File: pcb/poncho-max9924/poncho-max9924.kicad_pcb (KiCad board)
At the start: 2 copper layers, 48 parts, among them J1 Screw_Terminal_01x02, J2 Screw_Terminal_01x02, U1 MAX9924, U2 MAX9000

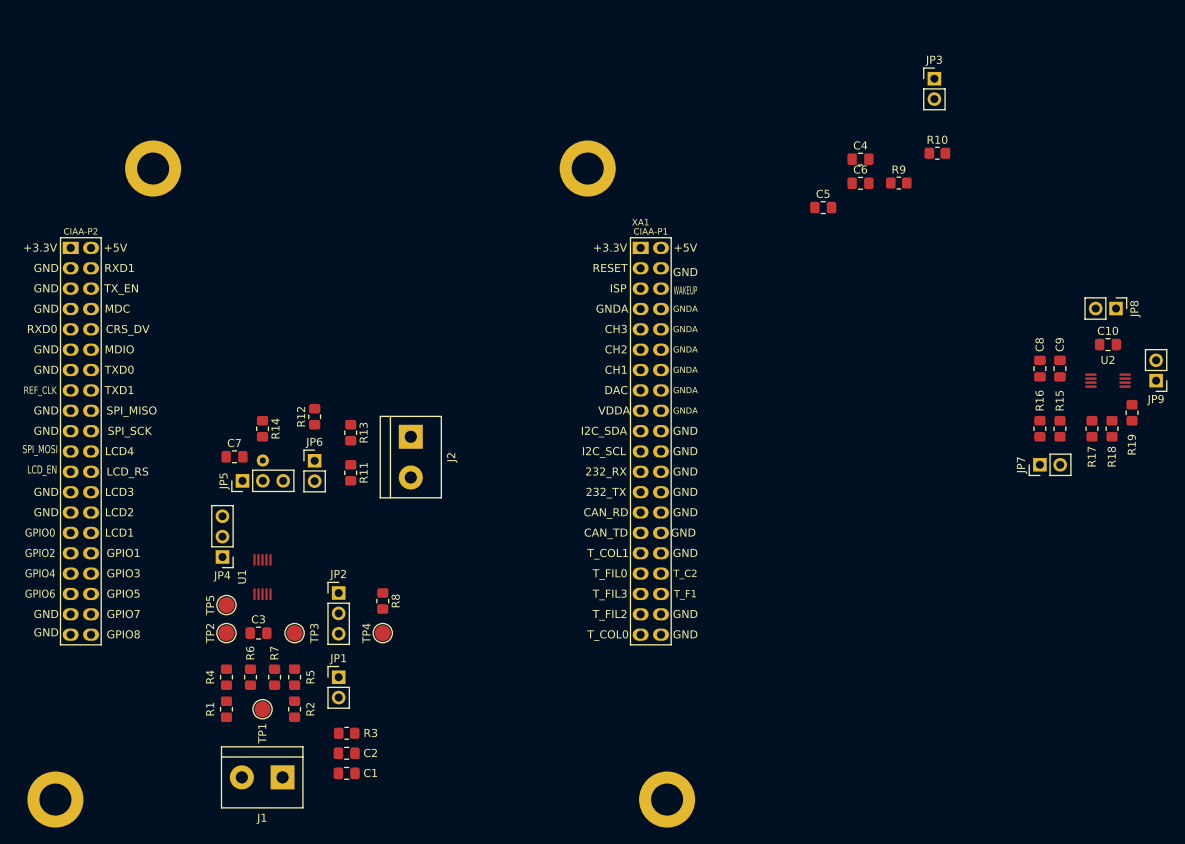
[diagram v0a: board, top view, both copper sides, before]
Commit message: Se agregaron modelos 3D de todos los componentes y sus footprints. Se re trabajo el posicionamiento de componentes en la placa.
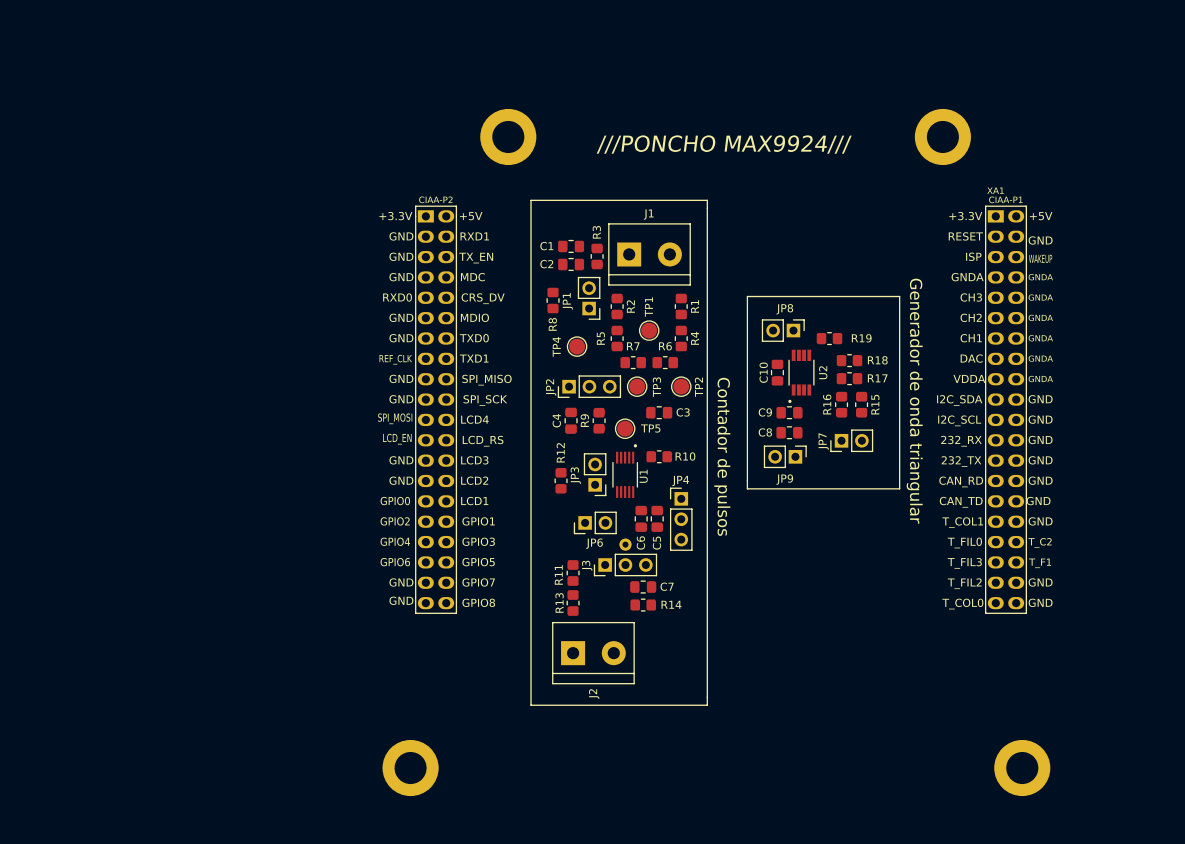
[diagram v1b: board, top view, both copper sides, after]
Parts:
- removed JP5: jumper_4_open, misc:PinHeader_1x03_1x01_P2.54mm_Vertical
- added J3: jumper_4_open, misc:PinHeader_1x03_1x01_P2.54mm_Vertical, F.Cu at (136.2, 112.5)
- U1: footprint umax:UMAX10 -> max9924:SOP50P490X110-10N
- U2: footprint umax:UMAX8 -> max9000:SOP65P490X110-8N
- moved J1 78.3 mm to (139.2, 73.8), turned to 0 degrees
- moved R1 75.8 mm to (145.8, 80.2), turned to 90 degrees
- moved C1 71.5 mm to (132.0, 72.8)
- moved R4 70.8 mm to (145.8, 84.2), turned to 90 degrees
- moved TP1 67.5 mm to (141.8, 83.2), turned to 270 degrees
- moved R3 67.2 mm to (135.2, 74.0), turned to 90 degrees
- moved C2 67.1 mm to (132.0, 75.0)
- moved JP3 66.0 mm to (135.0, 102.5), turned to 180 degrees
- moved R6 65.0 mm to (143.8, 87.2), turned to 180 degrees
- moved TP2 64.5 mm to (145.8, 90.2), turned to 270 degrees
- moved R2 64.4 mm to (137.8, 80.2), turned to 90 degrees
- moved R7 59.5 mm to (139.8, 87.2), turned to 180 degrees
- moved R5 58.4 mm to (137.8, 84.2), turned to 90 degrees
- moved JP4 57.7 mm to (145.8, 104.2), turned to 0 degrees
- moved C3 57.1 mm to (143.0, 93.5), turned to 180 degrees
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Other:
- board text added: "///PONCHO MAX9924///"
- board text added: "Contador de pulsos"
- board text added: "Generador de onda triangular"

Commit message: primer routeado
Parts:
- moved J1 21.4 mm to (144.5, 53.0), turned to 180 degrees
- moved J2 17.2 mm to (115.0, 123.5), turned to 270 degrees
- moved R14 4.47 mm to (137.0, 115.5), turned to 0 degrees
- moved R12 3.51 mm to (131.0, 98.5)
- moved C3 2.00 mm to (143.0, 95.5)
- moved R13 1.77 mm to (132.0, 115.5)
- moved TP3 1.75 mm to (142.0, 90.2)
- moved JP7 1.50 mm to (165.8, 98.5)
- moved R11 1.25 mm to (133.0, 112.5), turned to 0 degrees
- moved R10 1.12 mm to (144.0, 98.5), turned to 90 degrees
- moved C4 1.00 mm to (131.0, 94.5), turned to 90 degrees
- moved C10 0.79 mm to (157.0, 88.2)
- moved R17 0.35 mm to (166.5, 89.0)
- moved C7 0.25 mm to (141.0, 115.5)
- moved R18 0.25 mm to (166.5, 87.0), turned to 180 degrees
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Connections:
- R1 pad 2: Net-(J1-Pad2) -> Net-(J1-Pad1)
- R2 pad 2: Net-(J1-Pad1) -> Net-(J1-Pad2)
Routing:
- net GND: track 0.00 -> 47.3 mm, vias 0 -> 3
- net Net-(C3-Pad2): track 0.00 -> 42.1 mm
- net /AOUT: track 0.00 -> 32.6 mm
- net /COUT: track 0.00 -> 32.2 mm
- net /COUT_2: track 0.00 -> 28.3 mm
- net Net-(J1-Pad2): track 0.00 -> 26.9 mm
- net Net-(J1-Pad1): track 0.00 -> 26.8 mm
- net /BIAS: track 0.00 -> 25.3 mm
- net /FILTER: track 0.00 -> 22.0 mm
- net /V_PULL: track 0.00 -> 21.1 mm
- net Net-(C8-Pad2): track 0.00 -> 19.0 mm, vias 0 -> 2
- net +5V: track 0.00 -> 14.8 mm, vias 0 -> 1
- net Net-(C8-Pad1): track 0.00 -> 14.2 mm
- net Net-(R17-Pad1): track 0.00 -> 14.0 mm
- net Net-(JP4-Pad2): track 0.00 -> 13.3 mm
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- added copper zone on B.Cu, net +5V
- added copper zone on F.Cu, net GND
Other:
- board outline added: 86.4 x 96.5 mm
- board text added: "/////////////////// ///PONCHO MAX9924/// ///////////////////"
- board text added: "GND"
- board text added: "Material: FR4 Espesor: 1.6mm Componentes: Solo lado top. Serigrafia: Solo lado top, color: blanco. Grillas: 0.25mm, 0.5mm, 1mm"
- board text added: "Sensor Inductivo"
- board text added: "Tensión de bias"
- board text added: "V+"
- board text removed: "///PONCHO MAX9924///"

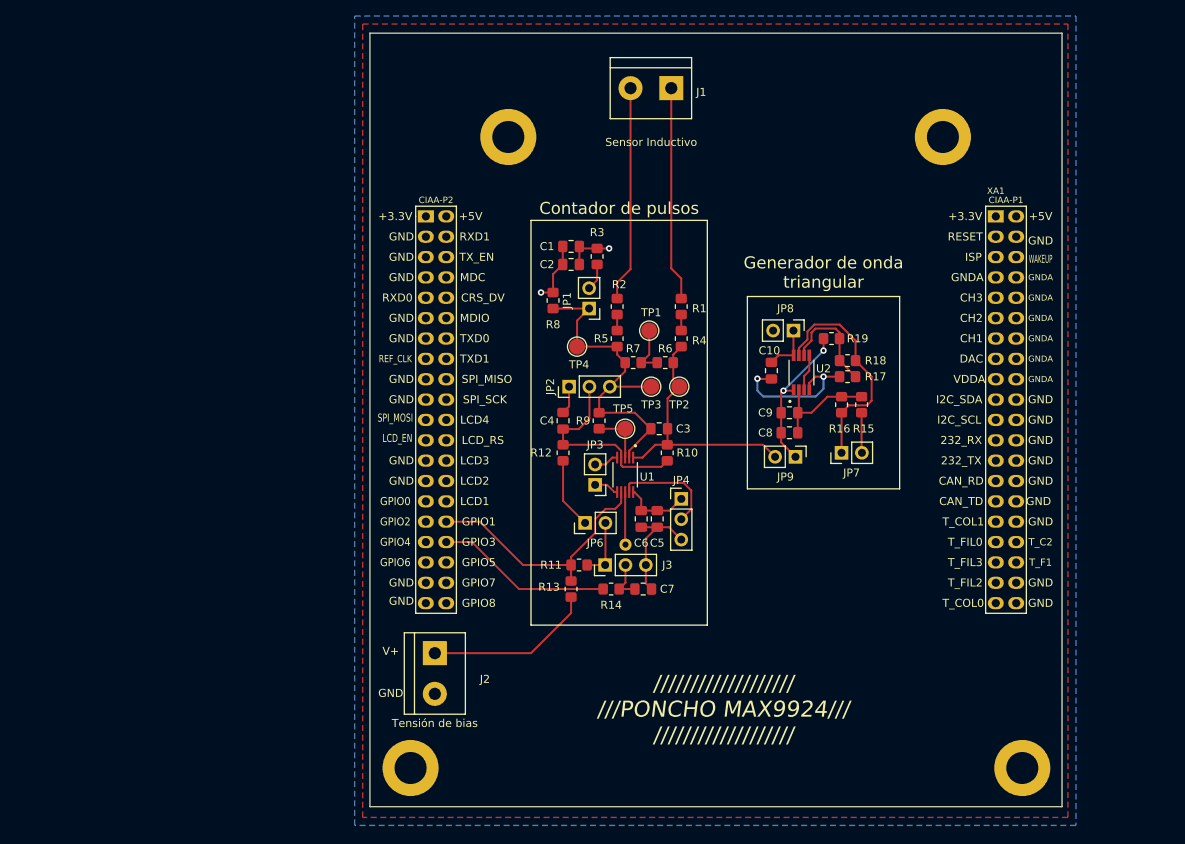
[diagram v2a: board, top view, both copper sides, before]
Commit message: correcciones y ruteo listo, falta hacer U2 multiparte
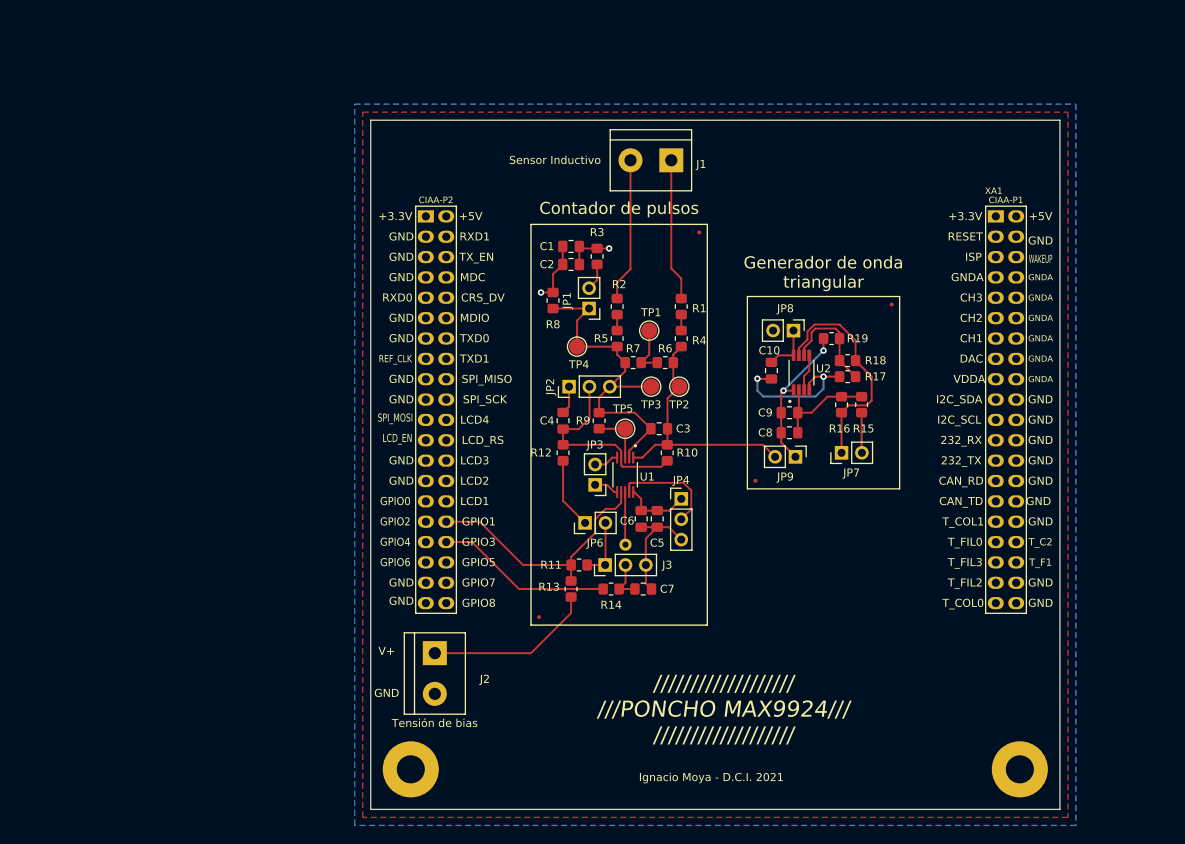
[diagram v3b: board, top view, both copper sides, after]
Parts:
- added FID1: Fiducial, Fiducial:Fiducial_0.5mm_Mask1mm, F.Cu at (148.0, 71.0)
- added FID2: Fiducial, Fiducial:Fiducial_0.5mm_Mask1mm, F.Cu at (128.0, 119.0)
- added FID3: Fiducial, Fiducial:Fiducial_0.5mm_Mask1mm, F.Cu at (172.0, 80.0)
- added FID4: Fiducial, Fiducial:Fiducial_0.5mm_Mask1mm, F.Cu at (155.0, 102.0)
- added H1: MountingHole, MountingHole:MountingHole_3.5mm_Pad, F.Cu at (188.0, 138.0)
- added H2: MountingHole, MountingHole:MountingHole_3.5mm_Pad, F.Cu at (112.0, 138.0)
- XA1: footprint Poncho_Esqueleto:Conn_Poncho_Mediano -> Poncho_Esqueleto:Conn_Poncho_SinBorde
- moved J1 9.00 mm to (144.5, 62.0)
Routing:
- net Net-(J1-Pad1): track 26.8 -> 17.8 mm
- net Net-(J1-Pad2): track 26.9 -> 17.9 mm
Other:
- board size 86.4 x 96.5 mm -> 86 x 86 mm
- board text added: "Ignacio Moya - D.C.I. 2021"
- board text added: "Material: FR4 Espesor: 1.6mm Componentes: Solo lado top. Serigrafia: Solo lado top, color: blanco. Color máscara antisoldante: verde. Grillas: 0.25mm, 0.5mm, 1mm"
- board text removed: "Material: FR4 Espesor: 1.6mm Componentes: Solo lado top. Serigrafia: Solo lado top, color: blanco. Grillas: 0.25mm, 0.5mm, 1mm"

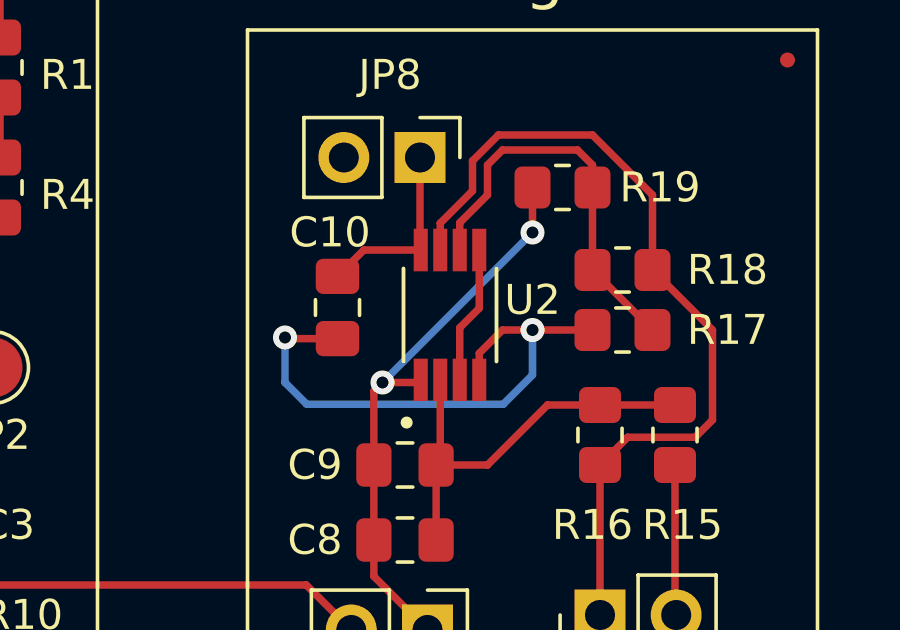
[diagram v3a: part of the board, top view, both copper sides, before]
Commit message: Se corrigieron errores en DRC y se agregó más info de fabricación en PCB
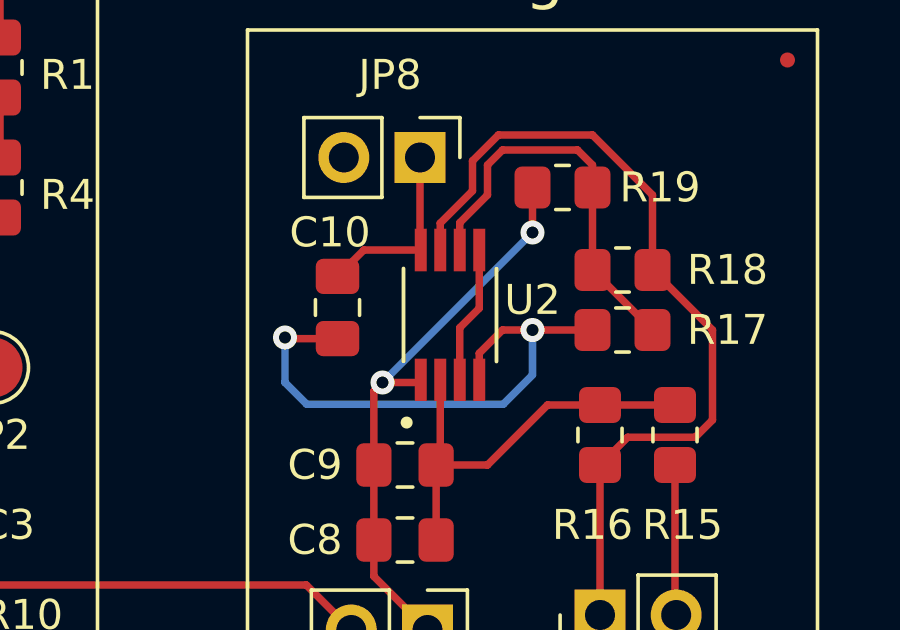
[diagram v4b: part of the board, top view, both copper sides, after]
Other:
- board text added: "Material: FR4 Terminación superficial: OSP Corte PCB: V-Scoring Espesor: 1.6mm Componentes: Solo lado top Serigrafia: Solo lado top, color: blanco Color máscara antisoldante: verde Grillas: 0.25mm, 0.5mm, 1mm"
- board text removed: "Material: FR4 Espesor: 1.6mm Componentes: Solo lado top. Serigrafia: Solo lado top, color: blanco. Color máscara antisoldante: verde. Grillas: 0.25mm, 0.5mm, 1mm"
